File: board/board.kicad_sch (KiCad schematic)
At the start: 5 parts, among them J1 002_SPI, J2 Conn_01x02_Male, J3 019_100BASE-T_with_CT

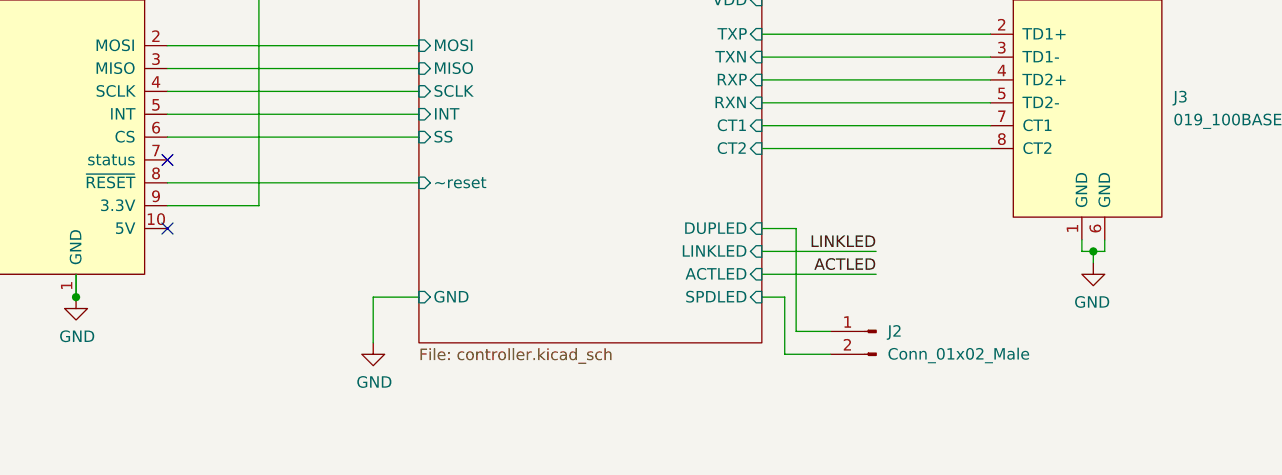
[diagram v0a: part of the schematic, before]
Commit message: broke out all leds in external connector
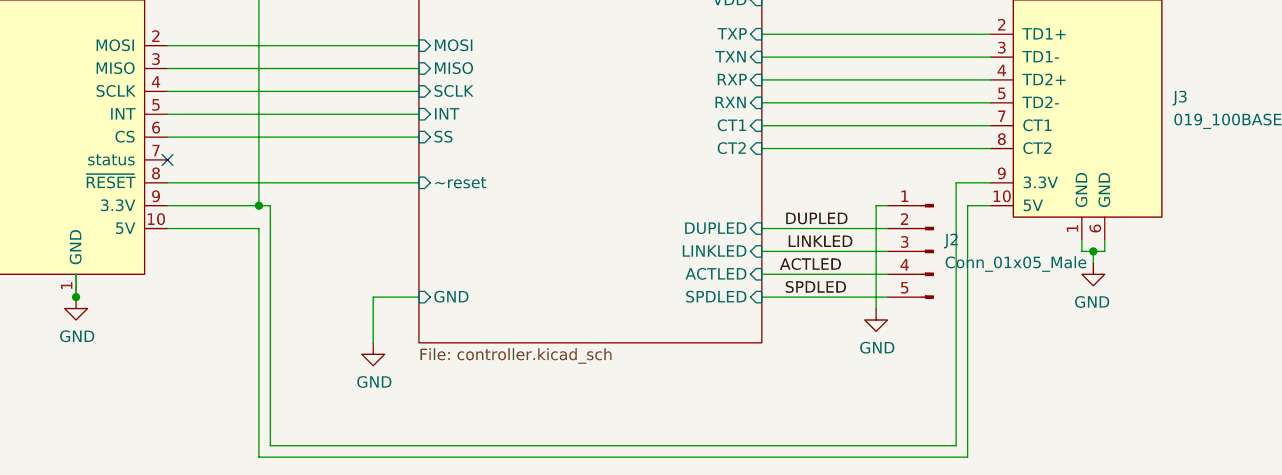
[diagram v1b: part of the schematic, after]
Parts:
- removed J2: Conn_01x02_Male, Connector_PinHeader_2.54mm:PinHeader_1x02_P2.54mm_Vertical, symbol Connector:Conn_01x02_Male
- added J2: Conn_01x05_Male, Connector_PinHeader_2.54mm:PinHeader_1x05_P2.54mm_Vertical, symbol Connector:Conn_01x05_Male
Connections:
- net ACTLED: now also J2.4 (Pin_4)
- net GND: now also J2.1 (Pin_1)
- net LINKLED: now also J2.3 (Pin_3)
- net at J1.10 (5V): now also J3.10 (5V)
- net +3V3 renamed +3.3V
- net +3.3V: now also J3.9 (3.3V)
- new net DUPLED: J2.2 (Pin_2)
- new net SPDLED: J2.5 (Pin_5)
- no-connect marks 2 -> 1
